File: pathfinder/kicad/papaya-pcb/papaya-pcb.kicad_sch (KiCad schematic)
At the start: 33 parts, among them J1 J1 (2 pins), J10 J_S2 (3 pins), J11 J_S3 (3 pins), J12 J_S4 (3 pins), J2 J_ESP32 (13 pins), J3 J_UBEC5V (4 pins), J4 J_BTS1 (6 pins), J5 J_BTS2 (6 pins), J6 J_ELRS (4 pins), J7 J_GND_MASTER (1 pins), J8 J_UBEC6V (2 pins), J9 J_S1 (3 pins), M1 Motor 1 (Right - Wheel 1), M2 Motor 2 (Left - Wheel 2), M3 Motor 3 (Right - Wheel 3), M4 Motor 4 (Left - Wheel 4), M5 Motor 5 (Right - Wheel 5), M6 Motor 6 (Left - Wheel 6), SW1 Main Power Switch, U1 UBEC 6V/8A, U2 UBEC 5V/3A

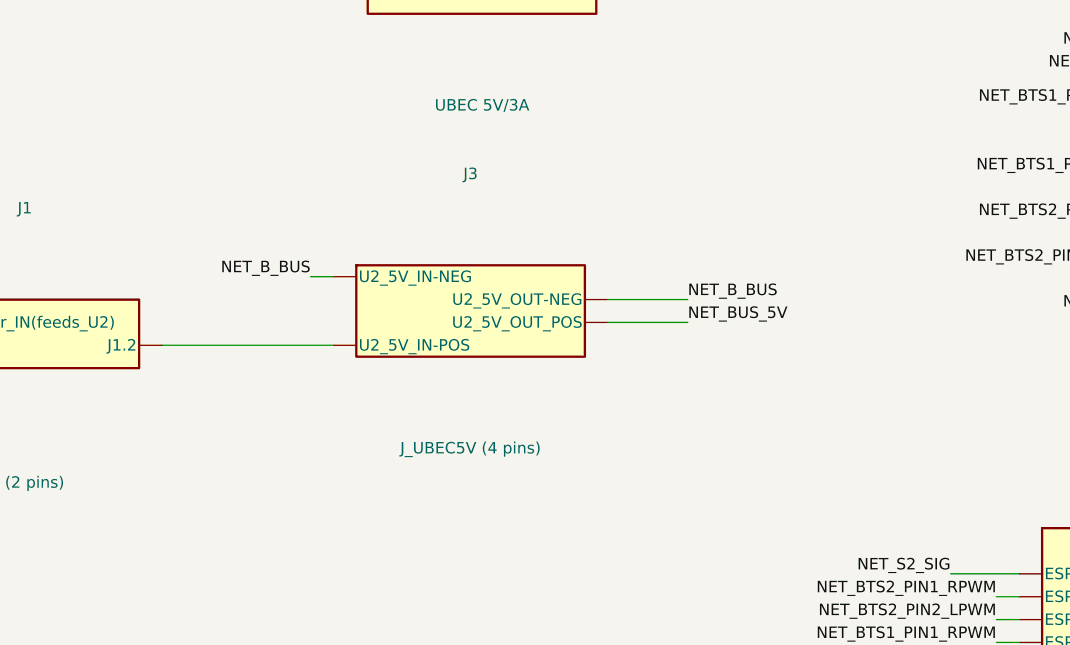
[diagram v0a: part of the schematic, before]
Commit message: Sync KiCad pin names to YAML; fix UBEC5V input net; add sync tooling
Added a kicad_sexpr.py (S-expression tokenizer/parser) and
sync_pin_names.py (pure text-patcher, insert-only so existing YAML
comments/formatting survive) to pull pin names tightened up in KiCad's
Symbol Editor back into papaya-wiring-layout.yaml as a new kicadPinName
field per connectionPoint, alongside the existing descriptive label.
generate_schematic.py now prefers kicadPinName when present.

Also fixes a real wiring bug found via netlist diff against the YAML:
J1 pin 2 (board ground-in) and J3 pin INP (UBEC 5V/3A positive input) had
been wired to each other instead of to their correct nets. Verified via
kicad-cli export against the YAML's expected nets -- all 20 nets now
match exactly.

Co-Authored-By: Claude Sonnet 5 <noreply@anthropic.com>
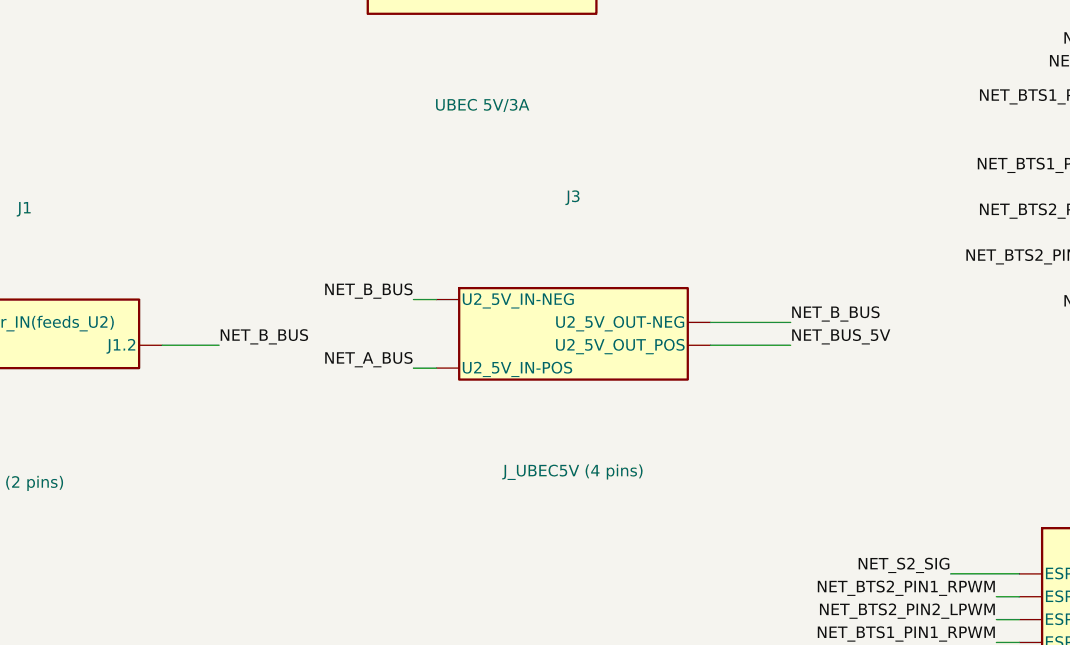
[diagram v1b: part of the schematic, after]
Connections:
- net NET_A_BUS: now also J3.INP (U2_5V_IN-POS)
- net NET_B_BUS: now also J1.2 (J1.2)
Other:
- moved on the sheet: J3
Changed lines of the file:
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@@
 	(wire
 		(pts
-			(xy 205.74 259.08) (xy 214.63 259.08)
+			(xy 217.17 261.62) (xy 226.06 261.62)
 		)
 		(stroke
@@
 	(wire
 		(pts
+			(xy 184.15 264.16) (xy 186.69 264.16)
+		)
+		(stroke
+			(width 0)
+			(type default)
+		)
+	)
+	(wire
+		(pts
 			(xy 176.53 220.98) (xy 167.64 220.98)
 		)
@@
 	(wire
 		(pts
-			(xy 205.74 256.54) (xy 214.63 256.54)
+			(xy 217.17 259.08) (xy 226.06 259.08)
 		)
 		(stroke
@@
 	(wire
 		(pts
-			(xy 156.21 261.62) (xy 175.26 261.62)
-		)
-		(stroke
-			(width 0)
-			(type default)
-		)
-	)
-	(wire
-		(pts
 			(xy 412.75 45.72) (xy 417.83 45.72)
 		)
@@
 	(wire
 		(pts
-			(xy 175.26 254) (xy 172.72 254)
+			(xy 186.69 256.54) (xy 184.15 256.54)
 		)
 		(stroke
@@
 	(wire
 		(pts
+			(xy 156.21 261.62) (xy 162.56 261.62)
+		)
+		(stroke
+			(width 0)
+			(type default)
+		)
+	)
+	(wire
+		(pts
 			(xy 175.26 113.03) (xy 181.61 113.03)
 		)
@@
 	)
 	(label "NET_BUS_5V"
-		(at 214.63 259.08 0)
+		(at 226.06 261.62 0)
 		(effects
 			(font
@@
 	)
 	(label "NET_B_BUS"
-		(at 172.72 254 180)
+		(at 184.15 256.54 180)
 		(effects
 			(font
@@
 		)
 	)
+	(label "NET_B_BUS"
+		(at 162.56 261.62 0)
+		(effects
+			(font
+				(size 1.27 1.27)
+			)
+			(justify left bottom)
+		)
+	)
 	(label "NET_BUS_5V"
 		(at 181.61 113.03 0)
@@
 		)
 	)
+	(label "NET_A_BUS"
+		(at 184.15 264.16 180)
+		(effects
+			(font
+				(size 1.27 1.27)
+			)
+			(justify right bottom)
+		)
+	)
 	(label "NET_RIGHT_POWER"
 		(at 374.65 50.8 180)
@@
 	)
 	(label "NET_B_BUS"
-		(at 214.63 256.54 0)
+		(at 226.06 259.08 0)
 		(effects
 			(font
@@
 	(symbol
 		(lib_id "AUTO:J3")
-		(at 190.5 257.81 0)
+		(at 201.93 260.35 0)
 		(unit 1)
 		(body_style 1)
@@
 		(dnp no)
 		(property "Reference" "J3"
-			(at 190.5 242.57 0)
+			(at 201.93 245.11 0)
 			(show_name no)
 			(do_not_autoplace no)
@@
 		)
 		(property "Value" "J_UBEC5V (4 pins)"
-			(at 190.5 273.05 0)
+			(at 201.93 275.59 0)
 			(show_name no)
 			(do_not_autoplace no)
@@
 		)
 		(property "Footprint" ""
-			(at 190.5 257.81 0)
+			(at 201.93 260.35 0)
 			(hide yes)
 			(show_name no)
@@
 		)
 		(property "Datasheet" ""
-			(at 190.5 257.81 0)
+			(at 201.93 260.35 0)
 			(hide yes)
 			(show_name no)
@@
 		)
 		(property "Description" ""
-			(at 190.5 257.81 0)
+			(at 201.93 260.35 0)
 			(show_name no)
 			(do_not_autoplace no)

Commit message: Assign real footprints to all board connectors; add BOM
Adds pathfinder/BOM.md with actual Amazon ASINs and measured dimensions
for the on-board parts (ESP32-S3 dev board, UBEC 5V/3A). Matched 11 of
12 board connectors against real footprints in the installed KiCad 10
library; the UBEC 5V/3A pads have no standard match, so built a custom
footprint (papaya-pcb.pretty/UBEC_5V_3A_10x15mm.kicad_mod) from measured
pin spacing, registered via a new project fp-lib-table, and corrected
its INP/INN/OUTP/OUTN pad placement per physical part orientation.

assign_footprints.py (new, insert-only text patcher like the other
sync tools) applied all 12 assignments directly to both the wiring YAML
(connector.footprint, for future regenerations) and the live schematic's
Footprint fields. generate_schematic.py now carries connector.footprint
through on regeneration. All assignments verified against a fresh
kicad-cli netlist export and ERC (0 real errors).

Co-Authored-By: Claude Sonnet 5 <noreply@anthropic.com>
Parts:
- J1, J7, J8: footprint (none) -> TerminalBlock:TerminalBlock_MaiXu_MX126-5.0-02P_1x02_P5.00mm
- J10, J11, J12, J9: footprint (none) -> Connector_PinHeader_2.54mm:PinHeader_1x03_P2.54mm_Vertical
- J2: footprint (none) -> Connector_PinSocket_2.54mm:PinSocket_2x22_P2.54mm_Vertical
- J3: footprint (none) -> papaya-pcb:UBEC_5V_3A_10x15mm
- J4, J5: footprint (none) -> Connector_PinHeader_2.54mm:PinHeader_1x06_P2.54mm_Vertical
- J6: footprint (none) -> Connector_PinHeader_2.54mm:PinHeader_1x04_P2.54mm_Vertical
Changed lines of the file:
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@@
 			)
 		)
-		(property "Footprint" ""
+		(property "Footprint" "Connector_PinSocket_2.54mm:PinSocket_2x22_P2.54mm_Vertical"
 			(at 284.48 304.8 0)
 			(hide yes)
@@
 			)
 		)
-		(property "Footprint" ""
+		(property "Footprint" "Connector_PinHeader_2.54mm:PinHeader_1x03_P2.54mm_Vertical"
 			(at 309.88 382.27 0)
 			(hide yes)
@@
 			)
 		)
-		(property "Footprint" ""
+		(property "Footprint" "Connector_PinHeader_2.54mm:PinHeader_1x03_P2.54mm_Vertical"
 			(at 224.79 381 0)
 			(hide yes)
@@
 			)
 		)
-		(property "Footprint" ""
+		(property "Footprint" "TerminalBlock:TerminalBlock_MaiXu_MX126-5.0-02P_1x02_P5.00mm"
 			(at 97.79 316.23 0)
 			(hide yes)
@@
 			)
 		)
-		(property "Footprint" ""
+		(property "Footprint" "Connector_PinHeader_2.54mm:PinHeader_1x04_P2.54mm_Vertical"
 			(at 64.77 260.35 0)
 			(hide yes)
@@
 			)
 		)
-		(property "Footprint" ""
+		(property "Footprint" "Connector_PinHeader_2.54mm:PinHeader_1x03_P2.54mm_Vertical"
 			(at 76.2 379.73 0)
 			(hide yes)
@@
 			)
 		)
-		(property "Footprint" ""
+		(property "Footprint" "TerminalBlock:TerminalBlock_MaiXu_MX126-5.0-02P_1x02_P5.00mm"
 			(at 274.32 166.37 0)
 			(hide yes)
@@
 			)
 		)
-		(property "Footprint" ""
+		(property "Footprint" "Connector_PinHeader_2.54mm:PinHeader_1x03_P2.54mm_Vertical"
 			(at 143.51 381 0)
 			(hide yes)
@@
 			)
 		)
-		(property "Footprint" ""
+		(property "Footprint" "papaya-pcb:UBEC_5V_3A_10x15mm"
 			(at 201.93 260.35 0)
 			(hide yes)
@@
 			)
 		)
-		(property "Footprint" ""
+		(property "Footprint" "Connector_PinHeader_2.54mm:PinHeader_1x06_P2.54mm_Vertical"
 			(at 165.1 162.56 0)
 			(hide yes)
@@
 			)
 		)
-		(property "Footprint" ""
+		(property "Footprint" "Connector_PinHeader_2.54mm:PinHeader_1x06_P2.54mm_Vertical"
 			(at 68.58 158.75 0)
 			(hide yes)
@@
 			)
 		)
-		(property "Footprint" ""
+		(property "Footprint" "TerminalBlock:TerminalBlock_MaiXu_MX126-5.0-02P_1x02_P5.00mm"
 			(at 140.97 261.62 0)
 			(hide yes)

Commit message: Replace ESP32 footprint with real split-header layout; add board outline
The library footprint (PinSocket_2x22, one compact block) was wrong for
this board -- the real ESP32-S3 dev board uses two separate 1x22 header
rows (Espressif's J1/J3) spaced across the board width, not one dual-row
connector. Built a custom footprint (ESP32S3_DevKit_2x1x22_split) with
all 44 physical positions for correct socket-strip fit, with the 13
actually-wired signals placed at their real positions per Espressif's
published ESP32-S3-DevKitC-1 pin tables (cross-checked against this
project's own early build notes -- the 5V/ground adjacencies matched
exactly). Row spacing (25.75mm) is the midpoint of a physical caliper
measurement (25.5-26.0mm) -- flagged for a final check before ordering
boards. Verified pin positions, no name collisions, and a clean
kicad-cli parse before applying.

Replaces the old footprint reference in the YAML, the live schematic's
J2 symbol, and assign_footprints.py's mapping so it won't regress.

Also includes the board outline and other in-progress PCB placement
work from the KiCad session.

Co-Authored-By: Claude Sonnet 5 <noreply@anthropic.com>
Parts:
- J2: footprint Connector_PinSocket_2.54mm:PinSocket_2x22_P2.54mm_Vertical -> papaya-pcb:ESP32S3_DevKit_2x1x22_split
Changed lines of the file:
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@@
 			)
 		)
-		(property "Footprint" "Connector_PinSocket_2.54mm:PinSocket_2x22_P2.54mm_Vertical"
+		(property "Footprint" "papaya-pcb:ESP32S3_DevKit_2x1x22_split"
 			(at 284.48 304.8 0)
 			(hide yes)
